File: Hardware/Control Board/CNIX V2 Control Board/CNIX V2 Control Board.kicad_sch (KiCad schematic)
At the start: 71 parts, among them J1 EXT, J10 LED, J11 USB_C_Receptacle, J3 Tube Out, J4 EXT, J5 I2C_ext, J6 Prog, J7 HT, J8 GND, J9 GND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

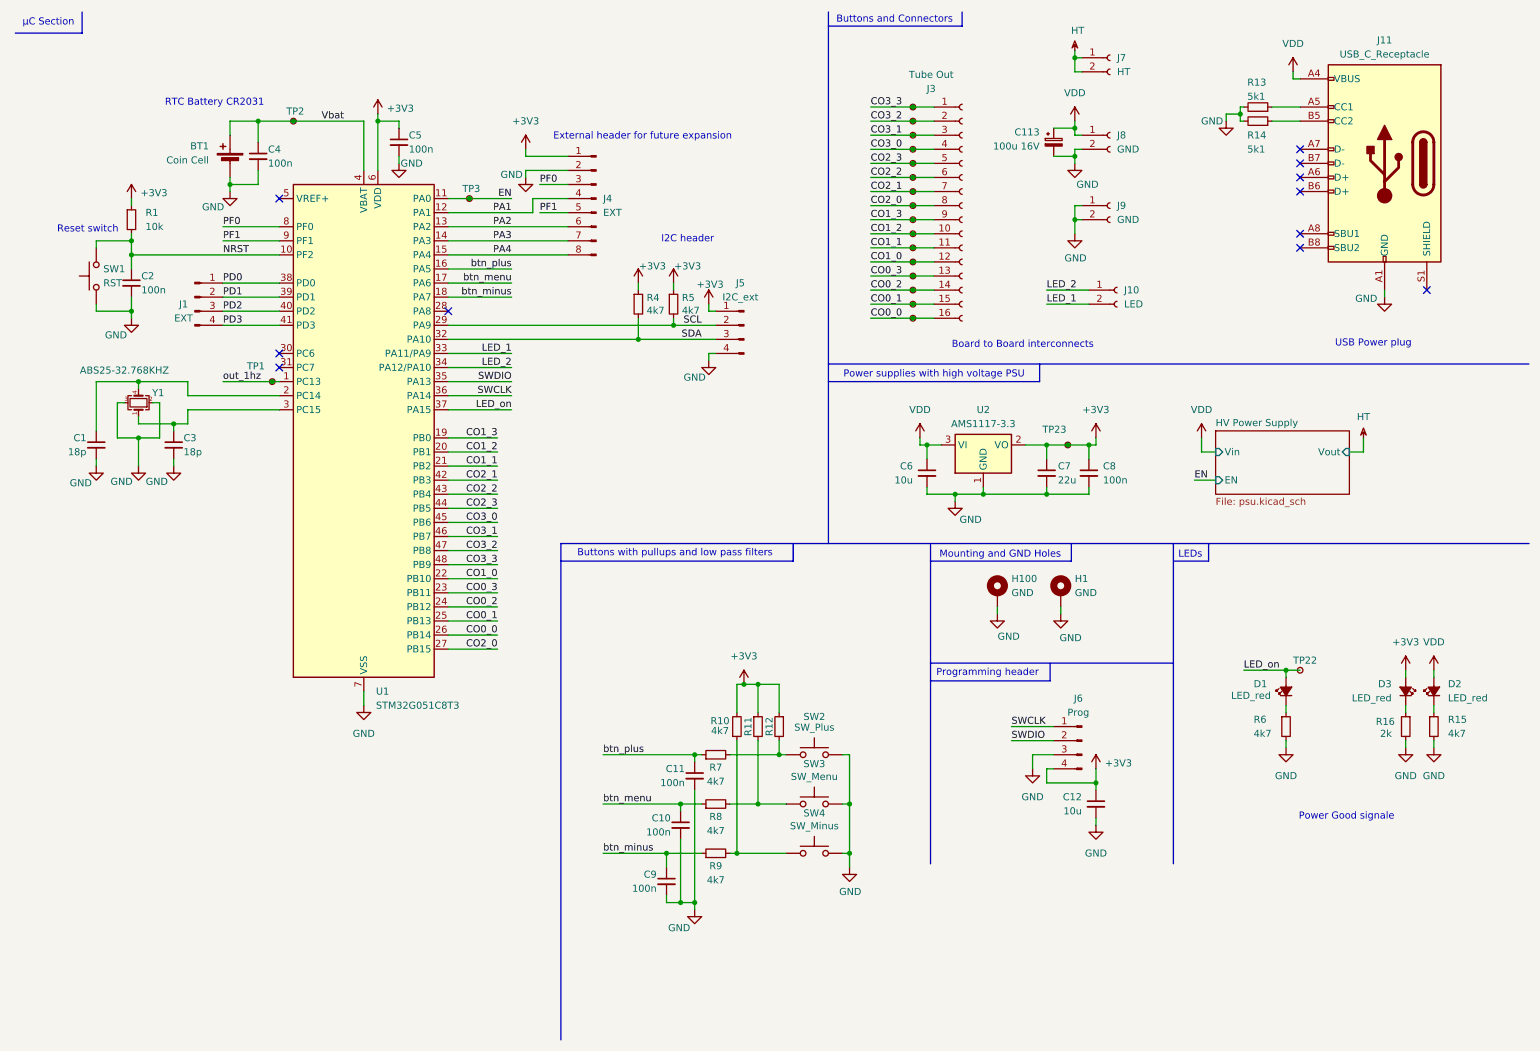
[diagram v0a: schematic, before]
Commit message: added bom and mouser nr
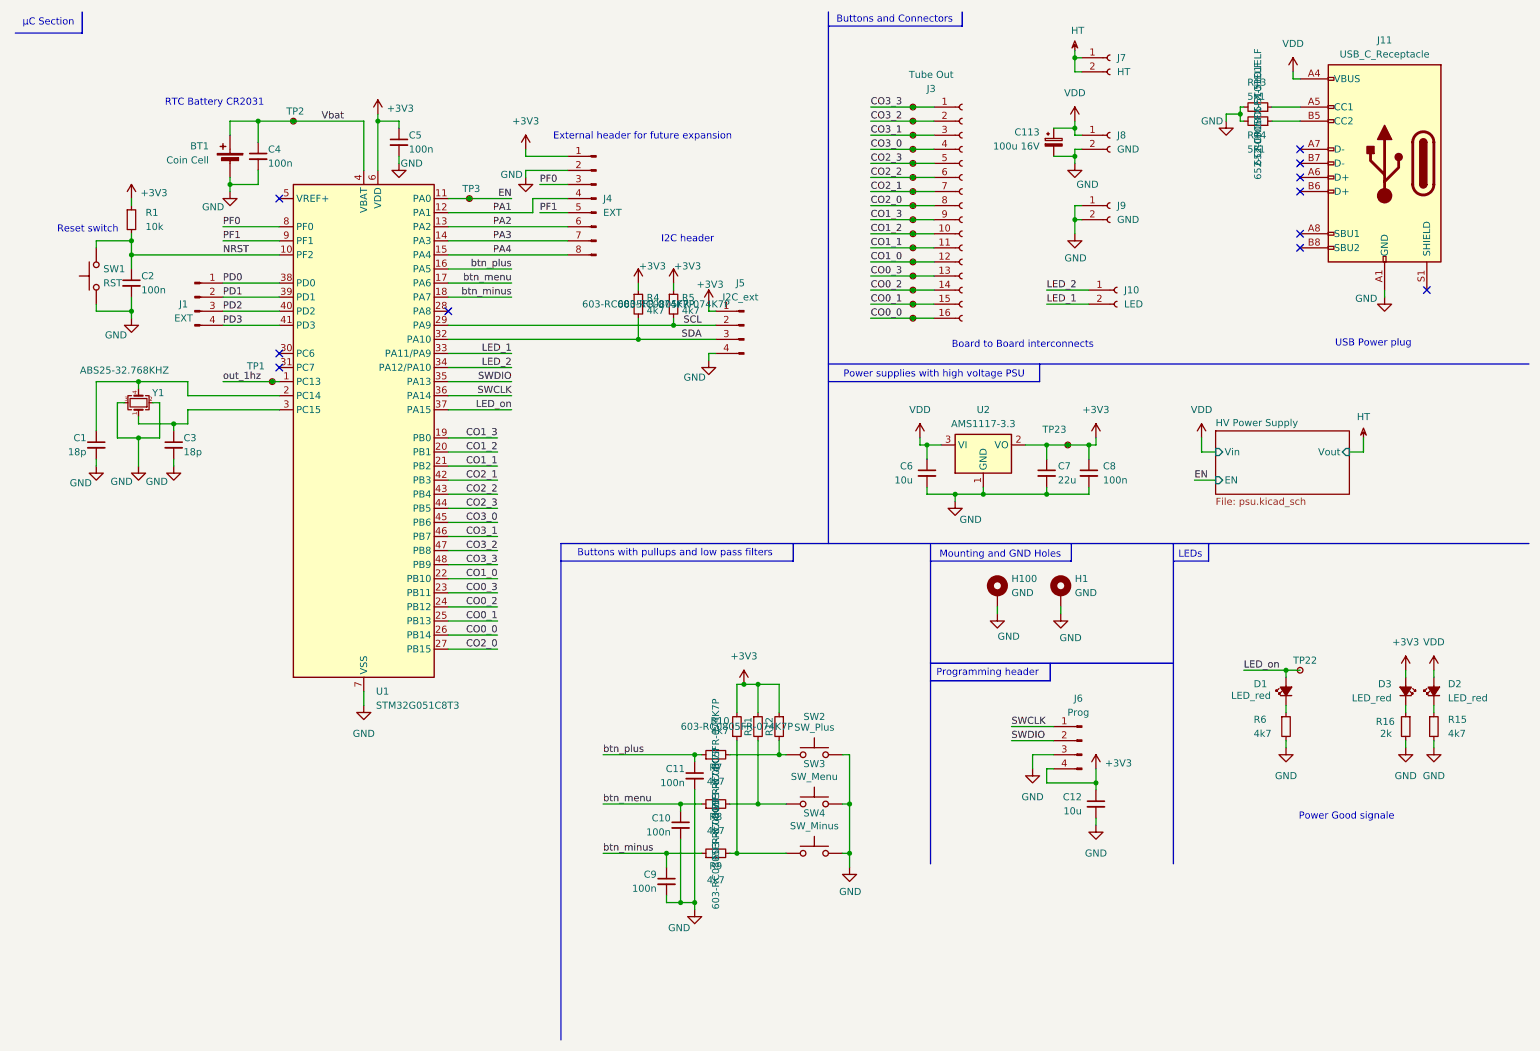
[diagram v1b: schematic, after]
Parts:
- C1, C3: Mouser Nr. (none) -> 80-C0805C180K5HACTU
- C12, C6: Mouser Nr. (none) -> 187-CL21B106KPQNNNE
- C7: Mouser Nr. (none) -> 187-CL21A226MQQNNNG
- R10, R11, R12, R15, R4, R5, R6, R7, R8, R9: Mouser Nr. (none) -> 603-RC0805FR-074K7P
- R13, R14: Mouser Nr. (none) -> 652-CR0805FX-5101ELF
- R16: Mouser Nr. (none) -> 603-RC0805FR-132KL

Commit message: Added TODOs and changed cap values for the LSE
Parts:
- C1, C3: value 18p -> 6p
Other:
- note added: "TODO: -Neuer µC, STM32H5 -> USB, RTC etc. -I2C Anschluss besseres Layout -Nirdrigere Cl für Crystal (DONE)"
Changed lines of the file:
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@@
 		)
 	)
+	(text "TODO: -Neuer µC, STM32H5 -> USB, RTC etc.\n	  -I2C Anschluss besseres Layout\n	  -Nirdrigere Cl für Crystal (DONE)"
+		(exclude_from_sim no)
+		(at 180.086 170.942 0)
+		(effects
+			(font
+				(size 1.27 1.27)
+			)
+			(justify left)
+		)
+	)
 	(text "Power supplies with high voltage PSU"
 		(exclude_from_sim no)
@@
 			)
 		)
-		(property "Value" "18p"
+		(property "Value" "6p"
 			(at 24.892 91.44 0)
 			(effects
@@
 			)
 		)
-		(property "Value" "18p"
+		(property "Value" "6p"
 			(at 42.418 91.44 0)
 			(effects

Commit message: Version bump 2.2.0 -> new regulator and id system
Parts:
- U2: value AMS1117-3.3 -> AP7361C-33ER-13; Mouser-Nr. (none) -> 621-AP7361C-33ER-13
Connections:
- net PD2 renamed id_bit0
- net PD3 renamed id_bit1
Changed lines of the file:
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@@
 		(title "Nixie Tube Clock")
 		(date "2024-10-17")
-		(rev "2.0")
+		(rev "2.2.0")
 		(company "C-Audio")
 	)
@@
 		)
 	)
-	(label "PD2"
+	(label "id_bit0"
 		(at 49.53 66.04 0)
 		(effects
@@
 		)
 	)
-	(label "PD3"
+	(label "id_bit1"
 		(at 49.53 68.58 0)
 		(effects
@@
 			)
 		)
-		(property "Value" "AMS1117-3.3"
+		(property "Value" "AP7361C-33ER-13"
 			(at 186.69 86.36 0)
 			(effects
@@
 			)
 		)
-		(property "Datasheet" "http://www.advanced-monolithic.com/pdf/ds1117.pdf"
+		(property "Datasheet" "https://www.mouser.de/datasheet/3/175/1/AP7361C.pdf"
 			(at 189.23 96.52 0)
 			(effects
@@
 			)
 		)
-		(property "Description" "1A Low Dropout regulator, positive, 3.3V fixed output, SOT-223"
+		(property "Description" "The AP7361C is a 1A, adjustable and fixed output voltage, ultra-low dropout linear regulator with enable. The device includes pass element, error amplifier, band-gap reference, current limit and thermal shutdown circuitry. The device is turned on when EN pin is set to logic high level."
 			(at 186.69 90.17 0)
 			(effects
@@
 			)
 		)
-		(property "Mouser-Nr." ""
+		(property "Mouser-Nr." "621-AP7361C-33ER-13 "
 			(at 186.69 90.17 0)
 			(effects
@@
 					(size 1.27 1.27)
 				)
+				(hide yes)
 			)
 		)
@@
 					(size 1.27 1.27)
 				)
+				(hide yes)
 			)
 		)

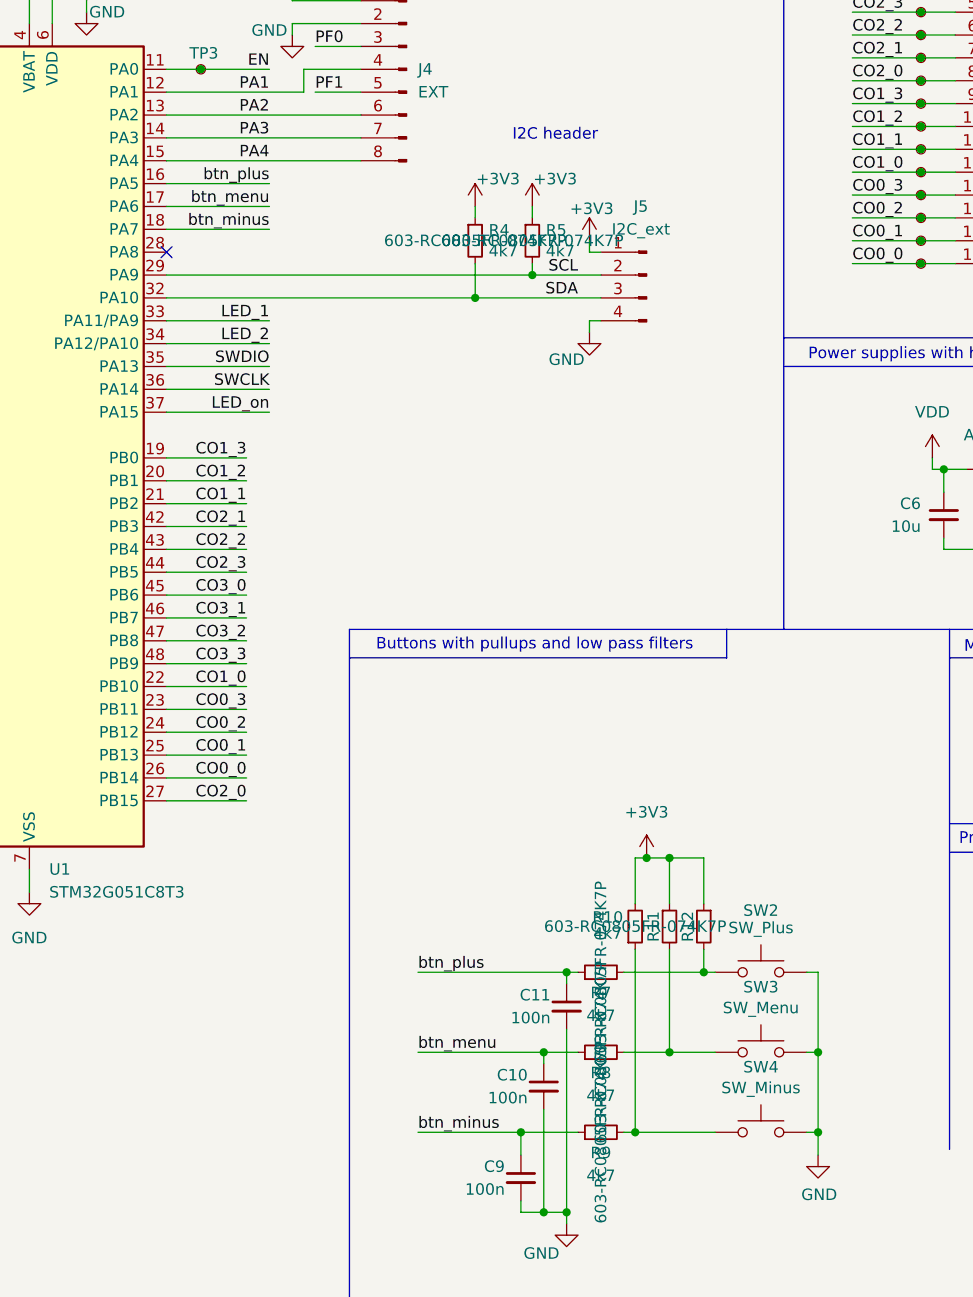
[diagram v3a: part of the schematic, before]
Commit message: updated firmware: implemented DHT22 sensor, addon board id check, menu structure, led blink display
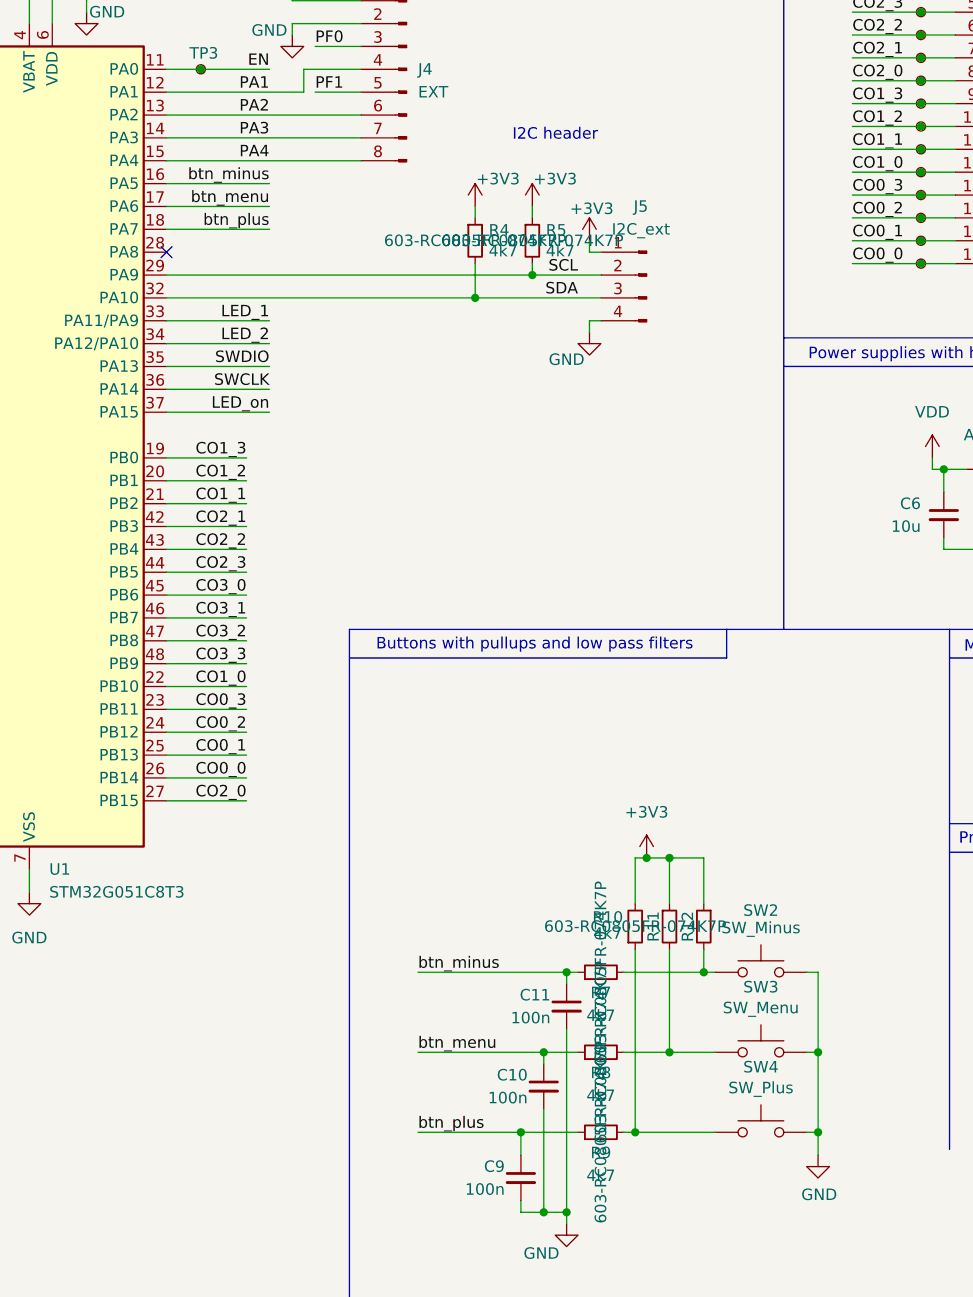
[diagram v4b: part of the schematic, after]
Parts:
- SW2: value SW_Plus -> SW_Minus
- SW4: value SW_Minus -> SW_Plus
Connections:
- net btn_minus: now also C11.1, R7.1, U1.16 (PA5); no longer C9.1, R9.1, U1.18 (PA7)
- net btn_plus: now also C9.1, R9.1, U1.18 (PA7); no longer C11.1, R7.1, U1.16 (PA5)
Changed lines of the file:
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@@
 	)
 	(label "btn_minus"
-		(at 118.11 163.83 0)
+		(at 118.11 146.05 0)
 		(effects
 			(font
@@
 	)
 	(label "btn_minus"
-		(at 101.6 63.5 180)
+		(at 101.6 58.42 180)
 		(effects
 			(font
@@
 	)
 	(label "btn_plus"
-		(at 101.6 58.42 180)
+		(at 101.6 63.5 180)
 		(effects
 			(font
@@
 	)
 	(label "btn_plus"
-		(at 118.11 146.05 0)
+		(at 118.11 163.83 0)
 		(effects
 			(font
@@
 			)
 		)
-		(property "Value" "SW_Plus"
+		(property "Value" "SW_Minus"
 			(at 156.21 141.1224 0)
 			(effects
@@
 			)
 		)
-		(property "Value" "SW_Minus"
+		(property "Value" "SW_Plus"
 			(at 156.21 158.9024 0)
 			(effects

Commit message: control board: added ht-psu enable jumper
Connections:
- net EN renamed ~{EN}
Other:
- sheet HV Power Supply ports: added ~{EN}; removed EN
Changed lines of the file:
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@@
 		)
 	)
+	(label "~{EN}"
+		(at 101.6 45.72 180)
+		(effects
+			(font
+				(size 1.27 1.27)
+			)
+			(justify right bottom)
+		)
+	)
 	(label "CO1_0"
 		(at 166.37 57.15 0)
@@
 		)
 	)
-	(label "EN"
-		(at 101.6 45.72 180)
-		(effects
-			(font
-				(size 1.27 1.27)
-			)
-			(justify right bottom)
-		)
-	)
 	(label "CO2_3"
 		(at 99.06 101.6 180)
@@
 		)
 	)
-	(label "EN"
+	(label "~{EN}"
 		(at 224.79 96.52 0)
 		(effects
@@
 			)
 		)
-		(pin "EN" input
+		(pin "~{EN}" input
 			(at 228.6 96.52 180)
 			(effects
